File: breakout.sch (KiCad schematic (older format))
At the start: 32 parts, among them CON1 SD_Card, CON2 USB-MICRO-AB, P2 CONN_01X40, P3 CONN_01X40, P4 CONN_01X40, P5 A-DF-09-A/KG-T4S, SW1 SW_PUSH

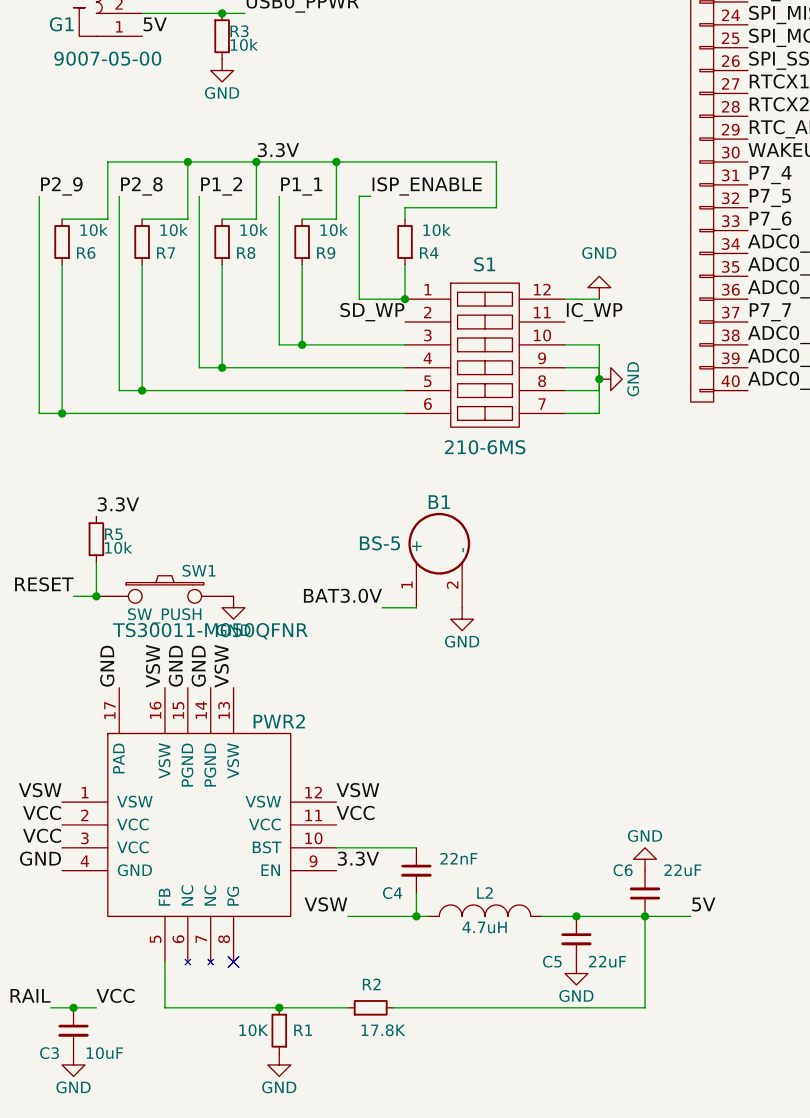
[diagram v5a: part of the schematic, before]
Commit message: traced 5V power regulator; removed uneeded components
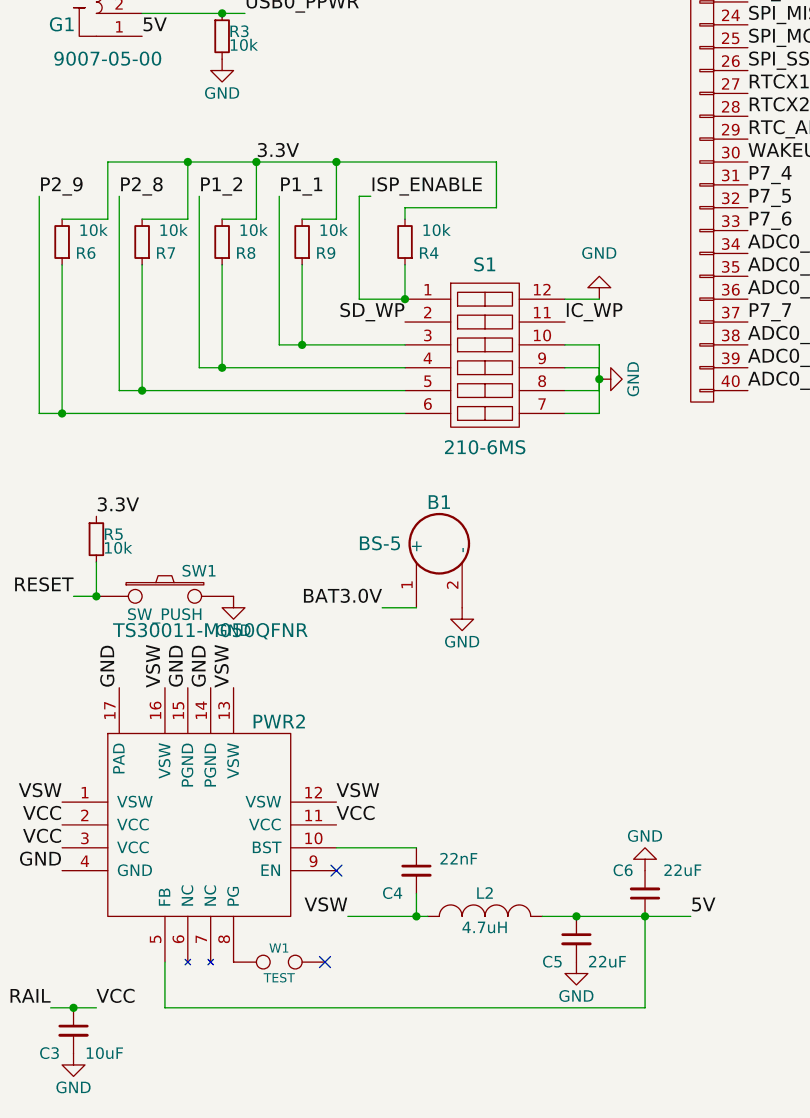
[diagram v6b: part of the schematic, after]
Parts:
- removed R1: 10K, Resistors_SMD:R_0402, symbol R_Small
- removed R2: 17.8K, Resistors_SMD:R_0402, symbol R_Small
- added W1: TEST, Measurement_Points:Measurement_Point_Round-SMD-Pad_Small, symbol TEST
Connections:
- net 3.3V: no longer PWR2.9 (EN)
- net 5V: now also PWR2.5 (FB)
- net at PWR2.8 (PG): now also W1.1
- no-connect marks 16 -> 17
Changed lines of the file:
@@
 Text Label 2000 9250 0    60   ~ 0
 VCC
-Text Label 2000 9450 0    60   ~ 0
-3.3V
 Text Label 1050 8650 1    60   ~ 0
 GND
@@
 	1    0    0    -1
 $EndComp
-NoConn ~ 1550 9850
-$Comp
-L R_Small R2
-U 1 1 561F82A3
-P 2150 10050
-F 0 "R2" V 2250 10000 50  0000 L CNN
-F 1 "17.8K" V 2050 9900 50  0000 L CNN
-F 2 "Resistors_SMD:R_0402" H 2150 10050 60  0001 C CNN
-F 3 "" H 2150 10050 60  0000 C CNN
-	1    2150 10050
-	0    -1   -1   0
-$EndComp
-$Comp
-L R_Small R1
-U 1 1 561F8304
-P 1750 10150
-F 0 "R1" H 1600 10150 50  0000 L CNN
-F 1 "10K" H 1800 10150 50  0000 L CNN
-F 2 "Resistors_SMD:R_0402" H 1750 10150 60  0001 C CNN
-F 3 "" H 1750 10150 60  0000 C CNN
-	1    1750 10150
-	-1   0    0    1
-$EndComp
-$Comp
-L GND #PWR011
-U 1 1 561F854B
-P 1750 10250
-F 0 "#PWR011" H 1750 10000 50  0001 C CNN
-F 1 "GND" H 1750 10100 50  0000 C CNN
-F 2 "" H 1750 10250 60  0000 C CNN
-F 3 "" H 1750 10250 60  0000 C CNN
-	1    1750 10250
-	1    0    0    -1
-$EndComp
+NoConn ~ 1950 9850
 $Comp
 L USB-MICRO-AB CON2
@@
 $EndComp
 $Comp
-L GND #PWR012
+L GND #PWR011
 U 1 1 56208A99
 P 1500 5900
-F 0 "#PWR012" H 1500 5650 50  0001 C CNN
+F 0 "#PWR011" H 1500 5650 50  0001 C CNN
 F 1 "GND" H 1500 5750 50  0000 C CNN
 F 2 "" H 1500 5900 60  0000 C CNN
@@
 $EndComp
 $Comp
-L GND #PWR013
+L GND #PWR012
 U 1 1 56282950
 P 3150 6950
-F 0 "#PWR013" H 3150 6700 50  0001 C CNN
+F 0 "#PWR012" H 3150 6700 50  0001 C CNN
 F 1 "GND" H 3150 6750 50  0000 C CNN
 F 2 "" H 3150 6950 60  0000 C CNN
@@
 $EndComp
 $Comp
-L GND #PWR014
+L GND #PWR013
 U 1 1 562864C0
 P 1550 8250
-F 0 "#PWR014" H 1550 8000 50  0001 C CNN
+F 0 "#PWR013" H 1550 8000 50  0001 C CNN
 F 1 "GND" H 1550 8100 50  0000 C CNN
 F 2 "" H 1550 8250 60  0000 C CNN
@@
 GND
 $Comp
-L GND #PWR015
+L GND #PWR014
 U 1 1 562880B7
 P 3150 7300
-F 0 "#PWR015" H 3150 7050 50  0001 C CNN
+F 0 "#PWR014" H 3150 7050 50  0001 C CNN
 F 1 "GND" H 3150 7150 50  0000 C CNN
 F 2 "" H 3150 7300 60  0000 C CNN
@@
 BAT3.0V
 $Comp
-L GND #PWR016
+L GND #PWR015
 U 1 1 563D5013
 P 2550 8300
-F 0 "#PWR016" H 2550 8050 50  0001 C CNN
+F 0 "#PWR015" H 2550 8050 50  0001 C CNN
 F 1 "GND" H 2550 8150 50  0000 C CNN
 F 2 "" H 2550 8300 60  0000 C CNN
@@
 Connection ~ 2350 9650
 Wire Wire Line
-	1250 10050 2050 10050
-Connection ~ 1750 10050
-Wire Wire Line
-	2250 10050 3350 10050
-Wire Wire Line
 	1150 5500 1350 5500
 Wire Wire Line
@@
 	1850 6600 2000 6600
 Wire Wire Line
-	2000 6350 2000 6600
+	2000 6600 2000 6350
 Wire Wire Line
 	1000 6350 2700 6350
@@
 Text Label 7650 7250 2    60   ~ 0
 RESET
+Wire Wire Line
+	1250 10050 3350 10050
+NoConn ~ 2000 9450
+$Comp
+L TEST W1
+U 1 1 564546B8
+P 1750 9850
+F 0 "W1" H 1750 9910 40  0000 C CNN
+F 1 "TEST" H 1750 9780 40  0000 C CNN
+F 2 "Measurement_Points:Measurement_Point_Round-SMD-Pad_Small" H 1750 9850 60  0001 C CNN
+F 3 "" H 1750 9850 60  0000 C CNN
+	1    1750 9850
+	1    0    0    -1
+$EndComp
 $EndSCHEMATC

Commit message: layed out the power domain
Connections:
- net GND: now also POWER1.1 (P1); no longer POWER1.2 (P2)
- net RAIL: now also POWER1.2 (P2); no longer POWER1.1 (P1)
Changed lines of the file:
@@
 	1    0    0    -1
 $EndComp
+Text Label 1600 750  0    60   ~ 0
+GND
 Text Label 1600 850  0    60   ~ 0
-GND
-Text Label 1600 750  0    60   ~ 0
 RAIL
 Text Label 4850 5500 2    60   ~ 0

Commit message: more decisions on component placement
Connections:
- net ADC0_2: no longer P3.39 (P39)
- net ADC0_3: no longer P3.36 (P36)
- net ADC0_4: no longer P3.35 (P35)
- net ADC0_5: no longer P3.40 (P40)
- net ADC0_6: no longer P3.38 (P38)
- net ADC0_7: no longer P3.34 (P34)
- net CLK2: no longer P3.4 (P4)
- net I2C0_SCL: no longer P2.39 (P39)
- net I2C0_SDA: no longer P2.40 (P40)
- net P1_0: no longer P2.1 (P1)
- net P1_1: no longer P2.3 (P3)
- net P1_14: no longer P2.14 (P14)
- net P1_15: no longer P2.15 (P15)
- net P1_16: no longer P2.17 (P17)
- net P1_17: no longer P2.19 (P19)
- net P1_18: no longer P2.20 (P20)
- net P1_19: no longer P2.21 (P21)
- net P1_2: no longer P2.4 (P4)
- net P1_20: no longer P2.23 (P23)
- net P1_3: no longer P2.5 (P5)
- net P1_5: no longer P2.8 (P8)
- net P1_7: no longer P2.9 (P9)
- net P1_8: no longer P2.10 (P10)
- net P2_10: no longer P3.9 (P9)
- net P2_11: no longer P3.10 (P10)
- net P2_12: no longer P3.11 (P11)
- net P2_13: no longer P3.12 (P12)
- net P2_2: no longer P2.32 (P32)
- net P2_4: no longer P2.35 (P35)
- net P2_5: no longer P2.38 (P38)
- net P2_6: no longer P3.1 (P1)
- net P2_8: no longer P3.3 (P3)
- net P2_9: no longer P3.7 (P7)
- net P3_0: no longer P3.14 (P14)
- net P3_1: no longer P3.16 (P16)
- net P3_2: no longer P3.18 (P18)
- net P3_4: no longer P3.21 (P21)
- net P3_5: no longer P3.23 (P23)
- net P5_1: no longer P2.2 (P2)
- net P5_2: no longer P2.6 (P6)
- net P5_3: no longer P2.11 (P11)
- net P5_4: no longer P2.12 (P12)
- net P5_5: no longer P2.13 (P13)
- net P5_6: no longer P2.16 (P16)
- net P5_7: no longer P2.18 (P18)
- net P6_0: no longer P2.25 (P25)
- net P6_1: no longer P2.26 (P26)
- net P6_10: no longer P3.5 (P5)
- net P6_11: no longer P3.6 (P6)
- net P6_12: no longer P3.8 (P8)
- net P6_2: no longer P2.27 (P27)
- net P6_3: no longer P2.28 (P28)
- net P6_4: no longer P2.29 (P29)
- net P6_5: no longer P2.30 (P30)
- net P6_6: no longer P2.31 (P31)
- net P6_7: no longer P2.33 (P33)
- net P6_8: no longer P2.34 (P34)
- net P6_9: no longer P3.2 (P2)
- net P7_0: no longer P3.13 (P13)
- net P7_1: no longer P3.15 (P15)
- net P7_2: no longer P3.17 (P17)
- net P7_3: no longer P3.19 (P19)
- net P7_4: no longer P3.31 (P31)
- net P7_5: no longer P3.32 (P32)
- net P7_6: no longer P3.33 (P33)
- net P7_7: no longer P3.37 (P37)
- net P9_5: no longer P2.22 (P22)
- net P9_6: no longer P2.24 (P24)
- net PF_4: no longer P3.22 (P22)
- net RTCX1: no longer P3.27 (P27)
- net RTCX2: no longer P3.28 (P28)
- net RTC_ALARM: no longer P3.29 (P29)
- net SPI_MISO: no longer P3.24 (P24)
- net SPI_MOSI: no longer P3.25 (P25)
- net SPI_SCK: no longer P3.20 (P20)
- net SPI_SSEL: no longer P3.26 (P26)
- net USB0_IND0: no longer P2.7 (P7)
- net USB1_D+: no longer P2.36 (P36)
- net USB1_D-: no longer P2.37 (P37)
- net WAKEUP0: no longer P3.30 (P30)
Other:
- moved on the sheet: P2, P3
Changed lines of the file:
@@
 L CONN_01X40 P3
 U 1 1 5614BAE0
-P 3600 5400
-F 0 "P3" H 3600 7450 50  0000 C CNN
-F 1 "CONN_01X40" V 3700 5400 50  0000 C CNN
-F 2 "Socket_Strips:Socket_Strip_Straight_1x40" H 3600 5400 60  0001 C CNN
-F 3 "" H 3600 5400 60  0000 C CNN
-	1    3600 5400
+P 3550 5400
+F 0 "P3" H 3550 7450 50  0000 C CNN
+F 1 "CONN_01X40" V 3650 5400 50  0000 C CNN
+F 2 "Socket_Strips:Socket_Strip_Straight_1x40" H 3550 5400 60  0001 C CNN
+F 3 "" H 3550 5400 60  0000 C CNN
+	1    3550 5400
 	-1   0    0    -1
 $EndComp
@@
 L CONN_01X40 P2
 U 1 1 5614BB79
-P 5600 700
-F 0 "P2" H 5600 2750 50  0000 C CNN
-F 1 "CONN_01X40" V 5700 700 50  0000 C CNN
-F 2 "Socket_Strips:Socket_Strip_Straight_1x40" H 5600 700 60  0001 C CNN
-F 3 "" H 5600 700 60  0000 C CNN
-	1    5600 700
+P 5600 650
+F 0 "P2" H 5600 2700 50  0000 C CNN
+F 1 "CONN_01X40" V 5700 650 50  0000 C CNN
+F 2 "Socket_Strips:Socket_Strip_Straight_1x40" H 5600 650 60  0001 C CNN
+F 3 "" H 5600 650 60  0000 C CNN
+	1    5600 650
 	0    1    -1   0
 $EndComp
